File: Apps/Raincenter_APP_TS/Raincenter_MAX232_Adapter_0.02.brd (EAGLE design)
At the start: 35 x 14.3 mm, 5 parts, among them IC101 MAX232ECSE

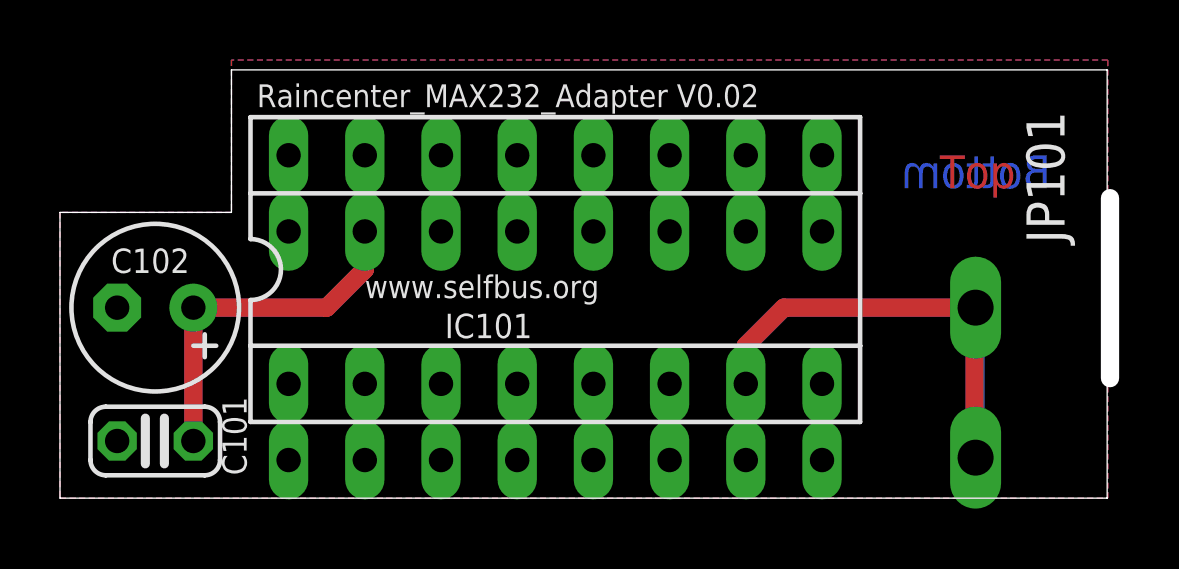
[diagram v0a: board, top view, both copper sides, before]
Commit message: Raincenter_APP updated combinded schematic and board (for cheaper production) of Raincenter_APP_TS_ARM_ISO_0.02 & Raincenter_MAX232_Adapter_0.02
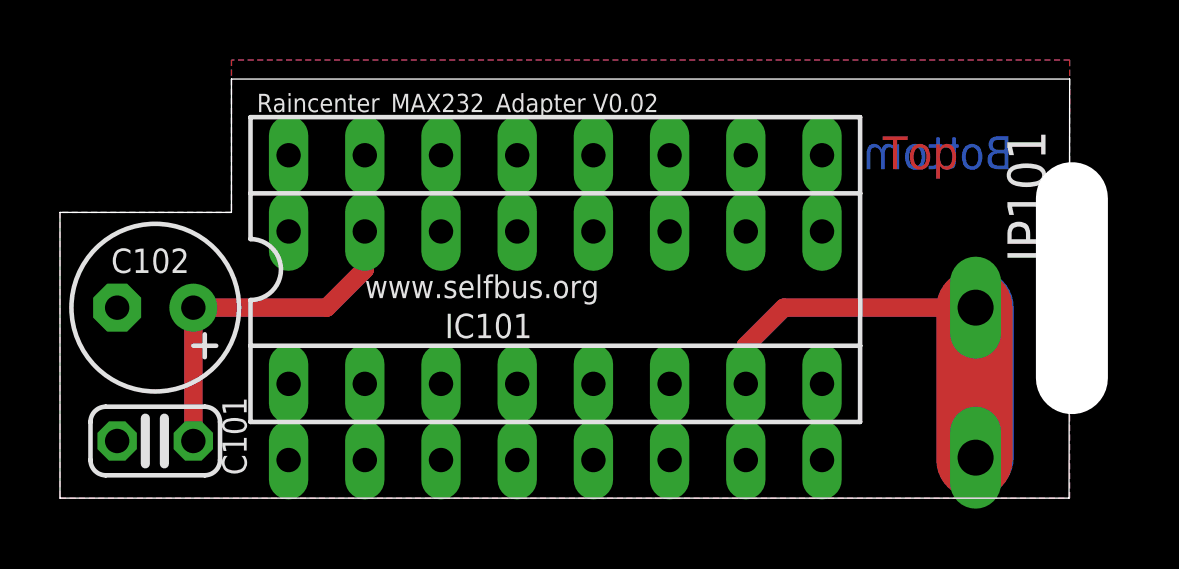
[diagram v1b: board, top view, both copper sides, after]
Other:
- board size 35 x 14.3 mm -> 33.7 x 14 mm
